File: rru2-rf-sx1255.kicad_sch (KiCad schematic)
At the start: 0 parts

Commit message: Add the basic SX1255 schematic and the footprints
- The SX1255 block, the ferrite bead supply and the ID EEPROM use the
  circuit of the SX1255 HAT: decoupling, TCXO clock into XTB, series
  resistors on SPI and I2S, test points on DIO0, DIO1 and DIO3.
- RX: U.FL, DC block and L match to RFI. TX: RFO_P through 33 pF to U.FL.
- Preliminary M.2 key E pinout (text on the schematic).
- Authors in the title blocks.
- The footprints are on the board. They are not placed and not routed.
- The board is marked as work in progress (KiCad text variable WIP_MARK).
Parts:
- added C1, C3, C38, C4: 1uF, Capacitor_SMD:C_0402_1005Metric, symbol M17_Passives:CAP-1U-25V-0402-X5R
- added C12, C14, C2, C30, C35, C7, C9: 100nF, Capacitor_SMD:C_0402_1005Metric, symbol M17_Passives:CAP-100N-50V-0402-X7R
- added C16: 33pF, Capacitor_SMD:C_0402_1005Metric, symbol M17_Passives:CAP-RF-33P-50V-0402-GJM
- added C20: 27pF, Capacitor_SMD:C_0402_1005Metric, symbol M17_Passives:CAP-RF-27P-50V-0402-GJM
- added C29: 10uF, Capacitor_SMD:C_0805_2012Metric, symbol M17_Passives:CAP-10U-50V-0805-X5R
- added C39, C61: 100pF, Capacitor_SMD:C_0402_1005Metric, symbol M17_Passives:CAP-RF-100P-100V-0402-GCM
- added FB1: 600R@100MHz, Inductor_SMD:L_0402_1005Metric, symbol M17_Passives:FB-600R-0402-BLM15PX
- added J1: M.2 key E, Connector_PCBEdge:M.2_2230-xx-E, symbol M17_Mechanical:CONN-M2-KEYE-2230-CARD
- added J2, J3: U.FL-R-SMT-1(60), Connector_Coaxial:U.FL_Hirose_U.FL-R-SMT-1_Vertical, symbol M17_Mechanical:CONN-UFL-HIROSE-R-SMT-1-60
- added L21: 39nH, Inductor_SMD:L_0402_1005Metric, symbol M17_Passives:IND-RF-39N-0402-LQW15AN00
- added L22: 82nH, Inductor_SMD:L_0402_1005Metric, symbol M17_Passives:IND-RF-82N-0402-LQW15AN00
- added R10, R11, R12, R13, R7, R8, R9: 120R, Resistor_SMD:R_0402_1005Metric, symbol M17_Passives:RES-120R-0402
- added R22, R23, R24: 10k, Resistor_SMD:R_0402_1005Metric, symbol M17_Passives:RES-10K-0402
- added TP1, TP2, TP3, TP4, TP5: TestPoint, TestPoint:TestPoint_Pad_D1.0mm, symbol M17_Mechanical:TP-PAD-1MM
- added U3: SX1255, Package_DFN_QFN:QFN-32-1EP_5x5mm_P0.5mm_EP3.3x3.3mm_ThermalVias, symbol M17_RF:SX1255IWLTRT
- added U6: AT24C32D, Package_TO_SOT_SMD:SOT-23-5, symbol M17_ICs:EEPROM-AT24C32D-STUM-T
- added Y1: 32MHz, Crystal:Crystal_SMD_2016-4Pin_2.0x1.6mm, symbol M17_ICs:TCXO-ECS-TXO-20CSMV4-32M
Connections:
- new net: C12.1, U3.3 (VR_ANAI)
- new net: TP3.1, U3.21 (DIO0)
- new net: R8.1, U3.19 (MOSI)
- new net: R13.1, U3.10 (CK_OUT)
- new net: R10.1, U3.17 (SCK)
- new net: R23.1, TP4.1, U6.5 (WP)
- new net: R7.1, U3.23 (DIO2)
- new net: TP2.1, U3.22 (DIO1)
- new net: C39.2, Y1.3 (OUT)
- new net: C39.1, U3.8 (XTB)
- new net: TP1.1, U3.24 (DIO3)
- new net: C20.1, U3.29 (RFO_{N})
- new net: R9.1, U3.18 (MISO)
- new net: C9.1, U3.5 (VR_DIG)
- new net: C61.1, J3.1 (In)
- new net: C7.1, U3.1 (VR_PA)
- new net: R12.1, U3.13 (I_IN)
- new net: R11.1, U3.15 (I_OUT)
- new net: C14.1, U3.25 (VR_ANA2)
- new net: C16.2, U3.30 (RFO_{P})
- new net: C61.2, L21.1
- new net +3V3: C35.1, FB1.1, J1.2 (3.3V), J1.4 (3.3V), J1.72 (3.3V), J1.74 (3.3V), R22.1, R23.2, R24.1, U6.4 (VCC)
- new net +3V3_RF: C1.1, C2.1, C29.1, C3.1, C30.1, C38.1, C4.1, FB1.2, U3.16 (VBAT), U3.2 (VBAT), U3.32 (VBAT), Y1.4 (VDD)
- new net GND: C1.2, C12.2, C14.2, C2.2, C20.2, C29.2, C3.2, C30.2, C35.2, C38.2, C4.2, C7.2, C9.2, J1.1 (GND), J1.18 (GND), J1.33 (GND), J1.39 (GND), J1.45 (GND), J1.51 (GND), J1.57 (GND), J1.63 (GND), J1.69 (GND), J1.7 (GND), J1.75 (GND), J2.2 (Ext), J3.2 (Ext), L22.2, TP5.1, U3.26 (GND), U3.28 (GND), U3.31 (GND), U3.33 (GND), U3.4 (GND), U3.7 (GND), U6.2 (GND), Y1.1 (GND), Y1.2 (GND)
- new net I2S_BCLK: J1.8 (PCM_CLK/I2S_SCK), R13.2
- new net I2S_RX: J1.12 (PCM_IN/I2S_SD_IN), R11.2
- new net I2S_TX: J1.14 (PCM_OUT/I2S_SD_OUT), R12.2
- new net I2S_WS: J1.10 (PCM_SYNC/I2S_WS), R7.2
- new net ID_SC: J1.40 (VENDOR_DEFINED), R24.2, U6.1 (SCL)
- new net ID_SD: J1.38 (VENDOR_DEFINED), R22.2, U6.3 (SDA)
- new net RX_SX1255: L21.2, L22.1, U3.27 (RFI)
- new net SPI_MISO: J1.13 (SDIO_DATA0), R9.2
- new net SPI_MOSI: J1.11 (SDIO_CMD), R8.2
- new net SPI_SCK: J1.9 (SDIO_CLK), R10.2
- new net SX_CS: J1.15 (SDIO_DATA1), U3.20 (~{CS})
- new net SX_RESET: J1.23 (~{SDIO_RESET}), U3.9 (RESET)
- new net TX_SX1255: C16.1, J2.1 (In)
- no-connect marks 0 -> 45
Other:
- note added: "${WIP_MARK}"
- note added: "M.2 key E card connector. Preliminary pinout."
- note added: "Preliminary M.2 key E pinout (standard names in brackets) Used now: 8 I2S_BCLK (PCM_CLK), 10 I2S_WS (PCM_SYNC) 12 I2S_RX (PCM_IN), 14 I2S_TX (PCM_OUT) 9 SPI_SCK (SDIO_CLK), 11 SPI_MOSI (SDIO_CMD) 13 SPI_MISO (SDIO_DATA0), 15 SX_CS (SDIO_DATA1) 23 SX_RESET (SDIO_RESET), 38 ID_SD, 40 ID_SC (VENDOR_DEFINED) Reserved for the next revision: 17 ATT_LE1, 19 ATT_LE2, 54 ATT_LE3 (PE4312) 56 PLL_LE, 62 PLL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"
- note added: "RX: U.FL, DC block, L match to RFI"
- note added: "TX: RFO_P through 33 pF to the U.FL"
- company: M17 Project -> M17 Foundation

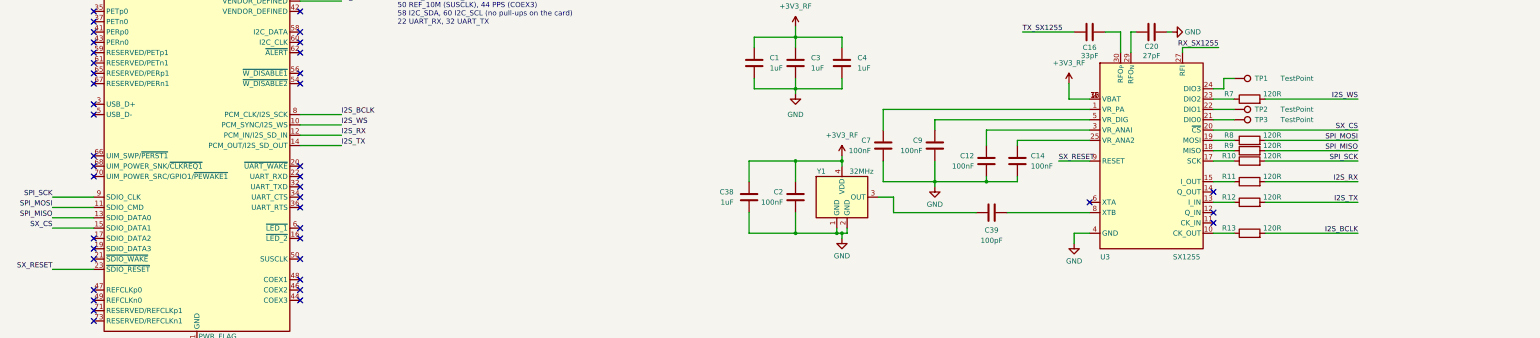
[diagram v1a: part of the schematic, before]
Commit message: Place the RF parts and add the 32 MHz VCXO
This is work in progress. The board has no tracks yet.

- Change the card size to M.2 2242 key E for the shield.
- Place the SX1255 near the middle of the card.
- Place the crystal, the capacitors and the supply filter near the SX1255.
- Put the two U.FL connectors near the screw end on opposite sides.
- Put the test pads on the bottom side.
- Add zones for the HMC374, the PE4312 attenuators and the ADF4002.
- Connect DIO0, DIO1 and DIO3 of the SX1255 to the M.2 pins 21, 20 and 16.
- Replace the TCXO with the Renesas XLH53V032 VCXO for the ADF4002 PLL.
- Add a 1k and 470R divider between the VCXO output and XTB.
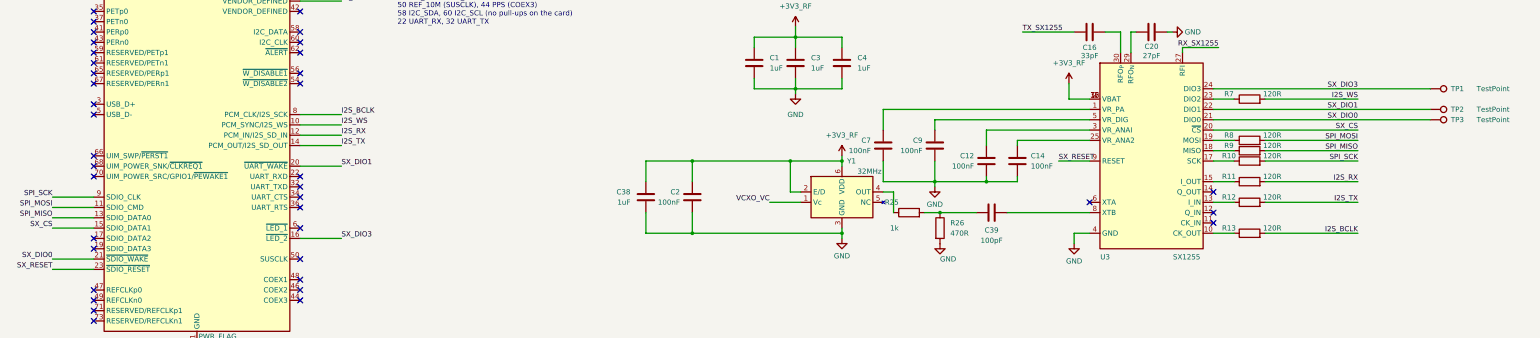
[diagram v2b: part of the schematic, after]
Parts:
- added R25: 1k, Resistor_SMD:R_0402_1005Metric, symbol M17_Passives:RES-1K-0402
- added R26: 470R, Resistor_SMD:R_0402_1005Metric, symbol M17_Passives:RES-470R-0402
- J1: footprint Connector_PCBEdge:M.2_2230-xx-E -> M17_Connectors:M.2_2242-xx-E; symbol M17_Mechanical:CONN-M2-KEYE-2230-CARD -> M17_Mechanical:CONN-M2-KEYE-2242-CARD
- Y1: footprint Crystal:Crystal_SMD_2016-4Pin_2.0x1.6mm -> Oscillator:Oscillator_SMD_IDT_JS6-6_5.0x3.2mm_P1.27mm; symbol M17_ICs:TCXO-ECS-TXO-20CSMV4-32M -> M17_ICs:VCXO-XLH53V032-32M; LCSC (none) -> C1671263; MPN ECS-TXO-20CSMV4-320-AY-TR -> XLH53V032.000000I; Manufacturer ECS Inc. -> Renesas Electronics; Mouser 520-TX20CSMV4320AYTR -> 972-XLH53V032000000I; Operating_temperature -30C-85C -> -40C-85C; Output clipped_sine_0.8Vpp_typ -> LVCMOS; Package 2.0x1.6mm -> 5.0x3.2mm; Pull_range (none) -> 50ppm_APR; Stability 0.5ppm -> (none); Supply_voltage 1.7V-3.6V -> 3.3V; Tuning_slope (none) -> 85ppm/V; Type tcxo -> vcxo
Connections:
- net +3V3_RF: now also Y1.2 (E/D), Y1.6 (VDD); no longer Y1.4 (VDD)
- net GND: now also Y1.3 (GND), R26.2; no longer Y1.1 (GND), Y1.2 (GND)
- net SX_DIO0: now reaches TP3.1, U3.21 (DIO0)
- net SX_DIO0: now also J1.21 (~{SDIO_WAKE})
- net SX_DIO1: now reaches TP2.1, U3.22 (DIO1)
- net SX_DIO1: now also J1.20 (~{UART_WAKE})
- net SX_DIO3: now reaches J1.16 (~{LED_2})
- net SX_DIO3: now also TP1.1, U3.24 (DIO3)
- net at C39.2: now also R25.2, R26.1; no longer Y1.3 (OUT)
- new net: R25.1, Y1.4 (OUT)
- new net VCXO_VC: Y1.1 (Vc)
- no-connect marks 45 -> 42
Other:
- moved on the sheet: C2, C38, TP1, TP2, TP3
